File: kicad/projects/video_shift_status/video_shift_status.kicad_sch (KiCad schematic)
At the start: 32 parts, among them J1 peripheral_addr_bus_connector, J2 peripheral_aux_connector, J3 peripheral_membank_connector, U1 74HC245, U10 74HC377, U11 74HC00, U12 74HC04, U2 74HC245, U3 74HC245, U4 74HC245, U5 74HC245, U6 74HC245, U7 74HC245, U8 74HC245, U9 74HC245

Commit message: Bit more tweaking and fleshing out of video circuits.
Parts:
- removed U11: 74HC00, symbol 74xx:74HC00
- removed U12: 74HC04, symbol 74xx:74HC04
- added C12, C13: C, Capacitor_THT:C_Disc_D5.0mm_W2.5mm_P5.00mm, symbol Device:C
- added J4, J5: Conn_01x16_Socket, Connector_PinSocket_2.54mm:PinSocket_1x16_P2.54mm_Horizontal, symbol Connector:Conn_01x16_Socket
- added U11: 74HC138, Package_DIP:DIP-16_W7.62mm_Socket, symbol sixteen-bit-computer:74HC138
- added U13: 74HC10, Package_DIP:DIP-14_W7.62mm_Socket, symbol sixteen-bit-computer:74HC10
- U10, U9: footprint (none) -> Package_DIP:DIP-20_W7.62mm_Socket
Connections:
- net ADDRESSED: now also U13.1, U13.9
- net GND: now also C12.2, C13.1, U11.3 (C), U11.4 (~{G2A}), U11.5 (~{G2B}), U11.8 (GND), U13.7 (GND)
- net MEM_ACT: now also U13.10, U13.2
- net SHIFT_SEL_0: now also U11.1 (A)
- net SHIFT_SEL_1: now also U11.2 (B)
- net VCC: now also C12.1, C13.2, U11.16 (VCC), U11.6 (G1), U13.14 (VCC), U13.4, U13.5
- net ~{READ}: now also U13.8
- net ~{RFM}/WTM: now also U13.13, U13.3
- net ~{WRITE}: now also U13.12
- net ~{SHIFT_2}: now reaches U3.19 (~{OE})
- net ~{SHIFT_2}: now also U7.19 (~{OE}), U11.13 (Y2)
- net ~{SHIFT_0}: now reaches U5.19 (~{OE})
- net ~{SHIFT_0}: now also U1.19 (~{OE}), U11.15 (Y0)
- net ~{SHIFT_1}: now reaches U2.19 (~{OE})
- net ~{SHIFT_1}: now also U6.19 (~{OE}), U11.14 (Y1)
- net ~{SHIFT_3}: now reaches U8.19 (~{OE})
- net ~{SHIFT_3}: now also U4.19 (~{OE}), U11.12 (Y3)
- net ADDR_BUS_00: no longer names the net of J1.17 (A_00)
- net ADDR_BUS_01: no longer names the net of J1.18 (A_01)
- net ADDR_BUS_02: no longer names the net of J1.19 (A_02)
- net ADDR_BUS_03: no longer names the net of J1.20 (A_03)
- net ADDR_BUS_04: no longer names the net of J1.21 (A_04)
- net ADDR_BUS_05: no longer names the net of J1.22 (A_05)
- net ADDR_BUS_06: no longer names the net of J1.23 (A_06)
- net ADDR_BUS_07: no longer names the net of J1.24 (A_07)
- net ADDR_BUS_08: no longer names the net of J1.25 (A_08)
- net ADDR_BUS_09: no longer names the net of J1.26 (A_09)
- net ADDR_BUS_10: no longer names the net of J1.27 (A_10)
- net ADDR_BUS_11: no longer names the net of J1.28 (A_11)
- net ADDR_BUS_12: no longer names the net of J1.29 (A_12)
- net ADDR_BUS_13: no longer names the net of J1.30 (A_13)
- net ADDR_BUS_14: no longer names the net of J1.31 (A_14)
- net ADDR_BUS_15: no longer names the net of J1.32 (A_15)
- net BANK_BUS_00: no longer names the net of J3.1 (B_00)
- net BANK_BUS_01: no longer names the net of J3.2 (B_01)
- net BANK_BUS_02: no longer names the net of J3.3 (B_02)
- net BANK_BUS_03: no longer names the net of J3.4 (B_03)
- net BANK_BUS_04: no longer names the net of J3.5 (B_04)
- net BANK_BUS_05: no longer names the net of J3.6 (B_05)
- net BANK_BUS_06: no longer names the net of J3.7 (B_06)
- net BANK_BUS_07: no longer names the net of J3.8 (B_07)
- net BANK_BUS_08: no longer names the net of J3.9 (B_08)
- net BANK_BUS_09: no longer names the net of J3.10 (B_09)
- net BANK_BUS_10: no longer names the net of J3.11 (B_10)
- net BANK_BUS_11: no longer names the net of J3.12 (B_11)
- net BANK_BUS_12: no longer names the net of J3.13 (B_12)
- net BANK_BUS_13: no longer names the net of J3.14 (B_13)
- net BANK_BUS_14: no longer names the net of J3.15 (B_14)
- net BANK_BUS_15: no longer names the net of J3.16 (B_15)
- net CTL_CLK: no longer names the net of J2.8 (CCLK)
- net DATA_BUS_05: no longer names the net of J1.6 (D_05)
- net DATA_BUS_06: no longer names the net of J1.7 (D_06)
- net DATA_BUS_07: no longer names the net of J1.8 (D_07)
- net DATA_BUS_08: no longer names the net of J1.9 (D_08)
- net DATA_BUS_09: no longer names the net of J1.10 (D_09)
- net DATA_BUS_10: no longer names the net of J1.11 (D_10)
- net DATA_BUS_11: no longer names the net of J1.12 (D_11)
- net DATA_BUS_12: no longer names the net of J1.13 (D_12)
- net DATA_BUS_13: no longer names the net of J1.14 (D_13)
- net DATA_BUS_14: no longer names the net of J1.15 (D_14)
- net DATA_BUS_15: no longer names the net of J1.16 (D_15)
- net RESET: no longer names the net of J2.14 (RST)
- new net RFM/~{WTM}: U13.11, U13.6
- no-connect marks 7 -> 56

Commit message: Adding video aux and some bits and bieces on video boards.
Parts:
- added C14, C15: C, Capacitor_THT:C_Disc_D5.0mm_W2.5mm_P5.00mm, symbol Device:C
- added J6: video_aux, Connector_PinSocket_2.54mm:PinSocket_1x07_P2.54mm_Horizontal, symbol sixteen-bit-computer:video_aux
- added J7: Conn_01x03_Pin, Connector_PinHeader_2.54mm:PinHeader_1x03_P2.54mm_Vertical, symbol Connector:Conn_01x03_Pin
- added J8: Conn_01x04_Socket, Connector_PinSocket_2.54mm:PinSocket_1x04_P2.54mm_Horizontal, symbol Connector:Conn_01x04_Socket
- added J9: Conn_02x06_Odd_Even, Connector_PinHeader_2.54mm:PinHeader_2x06_P2.54mm_Vertical, symbol Connector_Generic:Conn_02x06_Odd_Even
- added R2, R3, R4: 10K, Resistor_THT:R_Axial_DIN0207_L6.3mm_D2.5mm_P10.16mm_Horizontal, symbol Device:R_US
- added U12, U14: 74HC04, Package_DIP:DIP-14_W7.62mm_Socket, symbol 74xx:74HC04
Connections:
- net COL_IN_00 is gone; now on net COL_IN_0: U5.11 (B8)
- net COL_IN_01 is gone; now on net COL_IN_1: U5.12 (B7), U6.11 (B8)
- net COL_IN_02 is gone; now on net COL_IN_2: U5.13 (B6), U6.12 (B7), U7.11 (B8)
- net COL_IN_03 is gone; now on net COL_IN_3: U5.14 (B5), U6.13 (B6), U7.12 (B7), U8.11 (B8)
- net COL_IN_04 is gone; now on net COL_IN_4: U5.15 (B4), U6.14 (B5), U7.13 (B6), U8.12 (B7)
- net COL_IN_05 is gone; now on net COL_IN_5: U5.16 (B3), U6.15 (B4), U7.14 (B5), U8.13 (B6)
- net COL_IN_06 is gone; now on net COL_IN_6: U5.17 (B2), U6.16 (B3), U7.15 (B4), U8.14 (B5)
- net COL_IN_07 is gone; now on net COL_IN_7: U5.18 (B1), U6.17 (B2), U7.16 (B3), U8.15 (B4)
- net COL_OUT_00 is gone; now on net COL_OUT_0: U5.9 (A8), U6.9 (A8), U7.9 (A8), U8.9 (A8)
- net COL_OUT_01 is gone; now on net COL_OUT_1: U5.8 (A7), U6.8 (A7), U7.8 (A7), U8.8 (A7)
- net COL_OUT_02 is gone; now on net COL_OUT_2: U5.7 (A6), U6.7 (A6), U7.7 (A6), U8.7 (A6)
- net COL_OUT_03 is gone; now on net COL_OUT_3: U5.6 (A5), U6.6 (A5), U7.6 (A5), U8.6 (A5)
- net COL_OUT_04 is gone; now on net COL_OUT_4: U5.5 (A3), U6.5 (A3), U7.5 (A3), U8.5 (A3)
- net COL_OUT_05 is gone; now on net COL_OUT_5: U5.4 (A3), U6.4 (A3), U7.4 (A3), U8.4 (A3)
- net COL_OUT_06 is gone; now on net COL_OUT_6: U5.3 (A2), U6.3 (A2), U7.3 (A2), U8.3 (A2)
- net COL_OUT_07 is gone; now on net COL_OUT_7: U5.2 (A1), U6.2 (A1), U7.2 (A1), U8.2 (A1)
- net ROW_IN_00 is gone; now on net ROW_IN_0: U1.11 (B8)
- net ROW_IN_01 is gone; now on net ROW_IN_1: U1.12 (B7), U2.11 (B8)
- net ROW_IN_02 is gone; now on net ROW_IN_2: U1.13 (B6), U2.12 (B7), U3.11 (B8)
- net ROW_IN_03 is gone; now on net ROW_IN_3: U1.14 (B5), U2.13 (B6), U3.12 (B7), U4.11 (B8)
- net ROW_IN_04 is gone; now on net ROW_IN_4: U1.15 (B4), U2.14 (B5), U3.13 (B6), U4.12 (B7)
- net ROW_IN_05 is gone; now on net ROW_IN_5: U1.16 (B3), U2.15 (B4), U3.14 (B5), U4.13 (B6)
- net ROW_IN_06 is gone; now on net ROW_IN_6: U1.17 (B2), U2.16 (B3), U3.15 (B4), U4.14 (B5)
- net ROW_IN_07 is gone; now on net ROW_IN_7: U1.18 (B1), U2.17 (B2), U3.16 (B3), U4.15 (B4)
- net ROW_OUT_00 is gone; now on net ROW_OUT_0: U1.9 (A8), U2.9 (A8), U3.9 (A8), U4.9 (A8)
- net ROW_OUT_01 is gone; now on net ROW_OUT_1: U1.8 (A7), U2.8 (A7), U3.8 (A7), U4.8 (A7)
- net ROW_OUT_02 is gone; now on net ROW_OUT_2: U1.7 (A6), U2.7 (A6), U3.7 (A6), U4.7 (A6)
- net ROW_OUT_03 is gone; now on net ROW_OUT_3: U1.6 (A5), U2.6 (A5), U3.6 (A5), U4.6 (A5)
- net ROW_OUT_04 is gone; now on net ROW_OUT_4: U1.5 (A3), U2.5 (A3), U3.5 (A3), U4.5 (A3)
- net ROW_OUT_05 is gone; now on net ROW_OUT_5: U1.4 (A3), U2.4 (A3), U3.4 (A3), U4.4 (A3)
- net ROW_OUT_06 is gone; now on net ROW_OUT_6: U1.3 (A2), U2.3 (A2), U3.3 (A2), U4.3 (A2)
- net ROW_OUT_07 is gone; now on net ROW_OUT_7: U1.2 (A1), U2.2 (A1), U3.2 (A1), U4.2 (A1)
- net ADDRESSED: now also J8.1 (Pin_1), J8.2 (Pin_2), J8.3 (Pin_3), J8.4 (Pin_4), R4.2
- net BANK_SEL: now also U10.2 (Q0), J6.5 (BANK_SEL); no longer U10.15 (Q5)
- net DATA_BUS_00: now also U10.7 (D2); no longer U10.18 (D7)
- net DATA_BUS_01: now also U10.4 (D1); no longer U10.17 (D6)
- net DATA_BUS_02: now also U10.3 (D0); no longer U10.14 (D5)
- net GND: now also U10.14 (D5), U10.17 (D6), U10.18 (D7), C14.2, C15.2, R2.2, R3.2, R4.1, U12.3, U12.7 (GND), U14.7 (GND); no longer U10.3 (D0), U10.4 (D1), U10.7 (D2)
- net H_BLANK: now also J6.6 (H_BLANK)
- net SHIFT_SEL_0: now also U10.6 (Q2); no longer U10.19 (Q7)
- net SHIFT_SEL_1: now also U10.5 (Q1); no longer U10.16 (Q6)
- net VCC: now also C14.1, C15.1, U12.14 (VCC), U14.14 (VCC)
- net V_BLANK: now also J6.7 (V_BLANK)
- net ROW_OUT_0: now reaches J4.1 (Pin_1)
- net COL_OUT_1: now reaches J4.10 (Pin_10)
- net COL_OUT_2: now reaches J4.11 (Pin_11)
- net COL_OUT_3: now reaches J4.12 (Pin_12)
- net COL_OUT_4: now reaches J4.13 (Pin_13)
- net COL_OUT_5: now reaches J4.14 (Pin_14)
- net COL_OUT_6: now reaches J4.15 (Pin_15)
- net COL_OUT_7: now reaches J4.16 (Pin_16)
- net ROW_OUT_1: now reaches J4.2 (Pin_2)
- net ROW_OUT_2: now reaches J4.3 (Pin_3)
- net ROW_OUT_3: now reaches J4.4 (Pin_4)
- net ROW_OUT_4: now reaches J4.5 (Pin_5)
- net ROW_OUT_5: now reaches J4.6 (Pin_6)
- net ROW_OUT_6: now reaches J4.7 (Pin_7)
- net ROW_OUT_7: now reaches J4.8 (Pin_8)
- net COL_OUT_0: now reaches J4.9 (Pin_9)
- net ROW_IN_0: now reaches J5.1 (Pin_1)
- net COL_IN_1: now reaches J5.10 (Pin_10)
- net COL_IN_2: now reaches J5.11 (Pin_11)
- net COL_IN_3: now reaches J5.12 (Pin_12)
- net COL_IN_4: now reaches J5.13 (Pin_13)
- net COL_IN_5: now reaches J5.14 (Pin_14)
- net COL_IN_6: now reaches J5.15 (Pin_15)
- net COL_IN_7: now reaches J5.16 (Pin_16)
- net ROW_IN_1: now reaches J5.2 (Pin_2)
- net ROW_IN_2: now reaches J5.3 (Pin_3)
- net ROW_IN_3: now reaches J5.4 (Pin_4)
- net ROW_IN_4: now reaches J5.5 (Pin_5)
- net ROW_IN_5: now reaches J5.6 (Pin_6)
- net ROW_IN_6: now reaches J5.7 (Pin_7)
- net ROW_IN_7: now reaches J5.8 (Pin_8)
- net COL_IN_0: now reaches J5.9 (Pin_9)
- new net: U12.10, U12.9
- new net: U12.13, U12.6
- new net: U14.6, U14.9
- new net: U14.2, U14.3
- new net: U14.10, U14.13
- new net CHOSEN_PIX_CLK: J7.2 (Pin_2), J9.2 (Pin_2), R2.1, U12.5
- new net PIX_CLK_DELAY_1: J9.4 (Pin_4), U12.11, U12.12
- new net PIX_CLK_DELAY_2: J9.6 (Pin_6), U12.8, U14.1
- new net PIX_CLK_DELAY_3: J9.8 (Pin_8), U14.4, U14.5
- new net PIX_CLK_DELAY_4: J9.10 (Pin_10), U14.11, U14.8
- new net PIX_CLK_DELAY_5: J9.12 (Pin_12), U14.12
- new net PIX_CLK_MOD: J6.4 (PIX_CLK_MOD), J9.1 (Pin_1), J9.11 (Pin_11), J9.3 (Pin_3), J9.5 (Pin_5), J9.7 (Pin_7), J9.9 (Pin_9), R3.1
- new net PIX_CLK_RAW: J6.3 (PIX_CLK_RAW), J7.3 (Pin_3), U12.1
- new net ~{PIX_CLK_RAW}: J7.1 (Pin_1), U12.2
- no-connect marks 56 -> 59
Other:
- note added: "Addressed input"
- note added: "Pixel clock delay"
- note added: "Shift select"
- moved on the sheet: C1, C10, C11, C12, C13, C2, C3, C4, C5, C6, C7, C8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

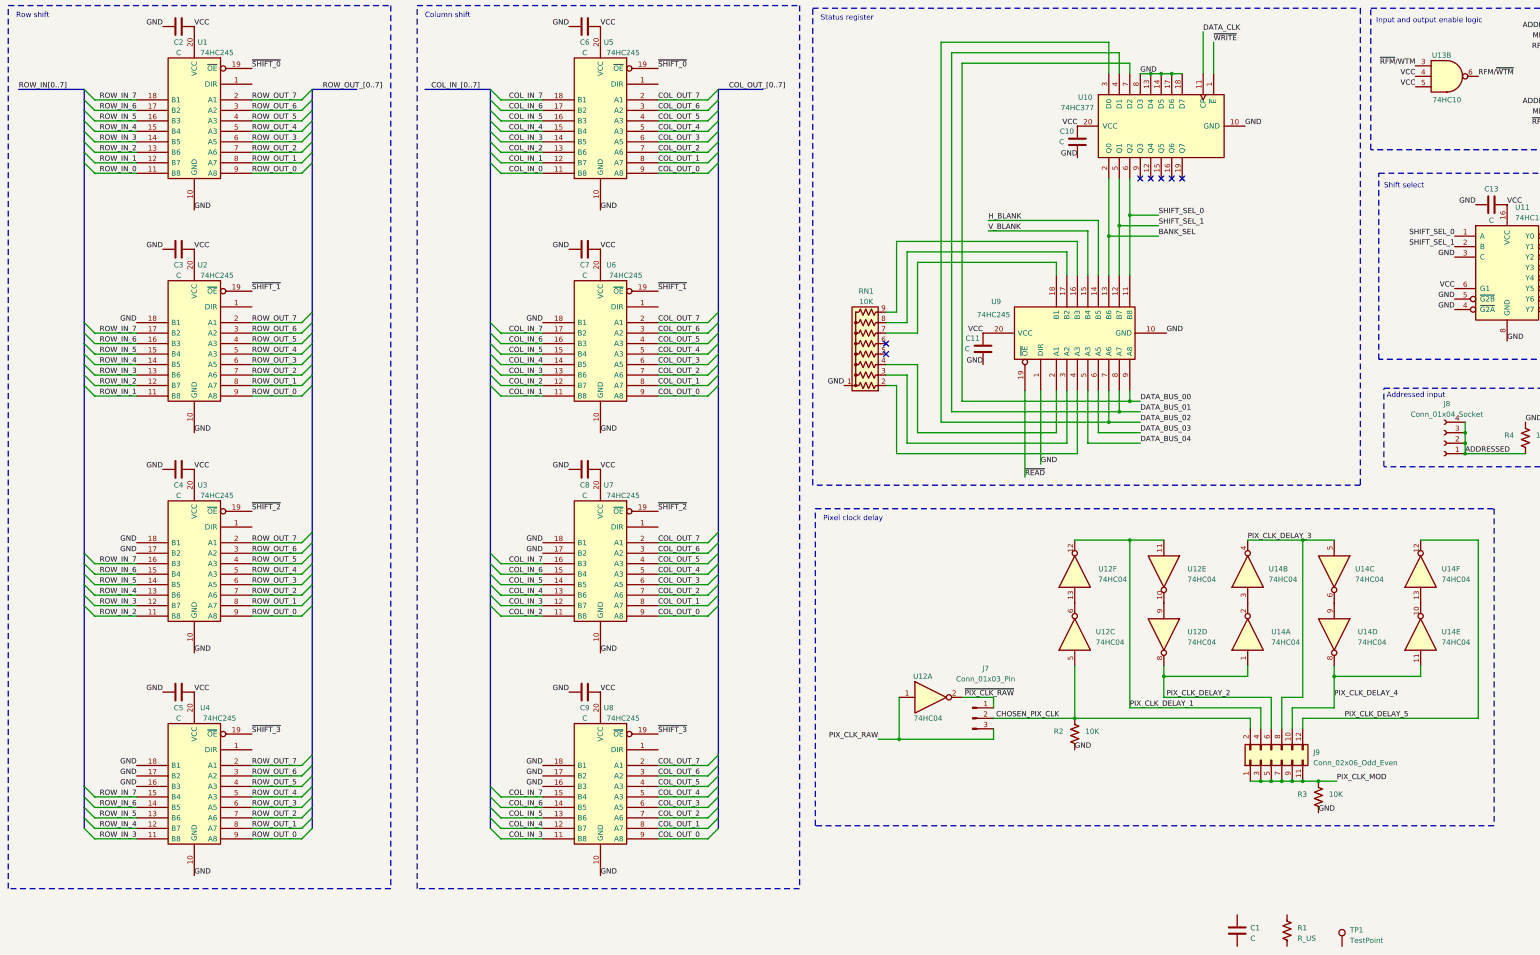
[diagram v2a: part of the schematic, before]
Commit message: Start work on shift status delay PCB.
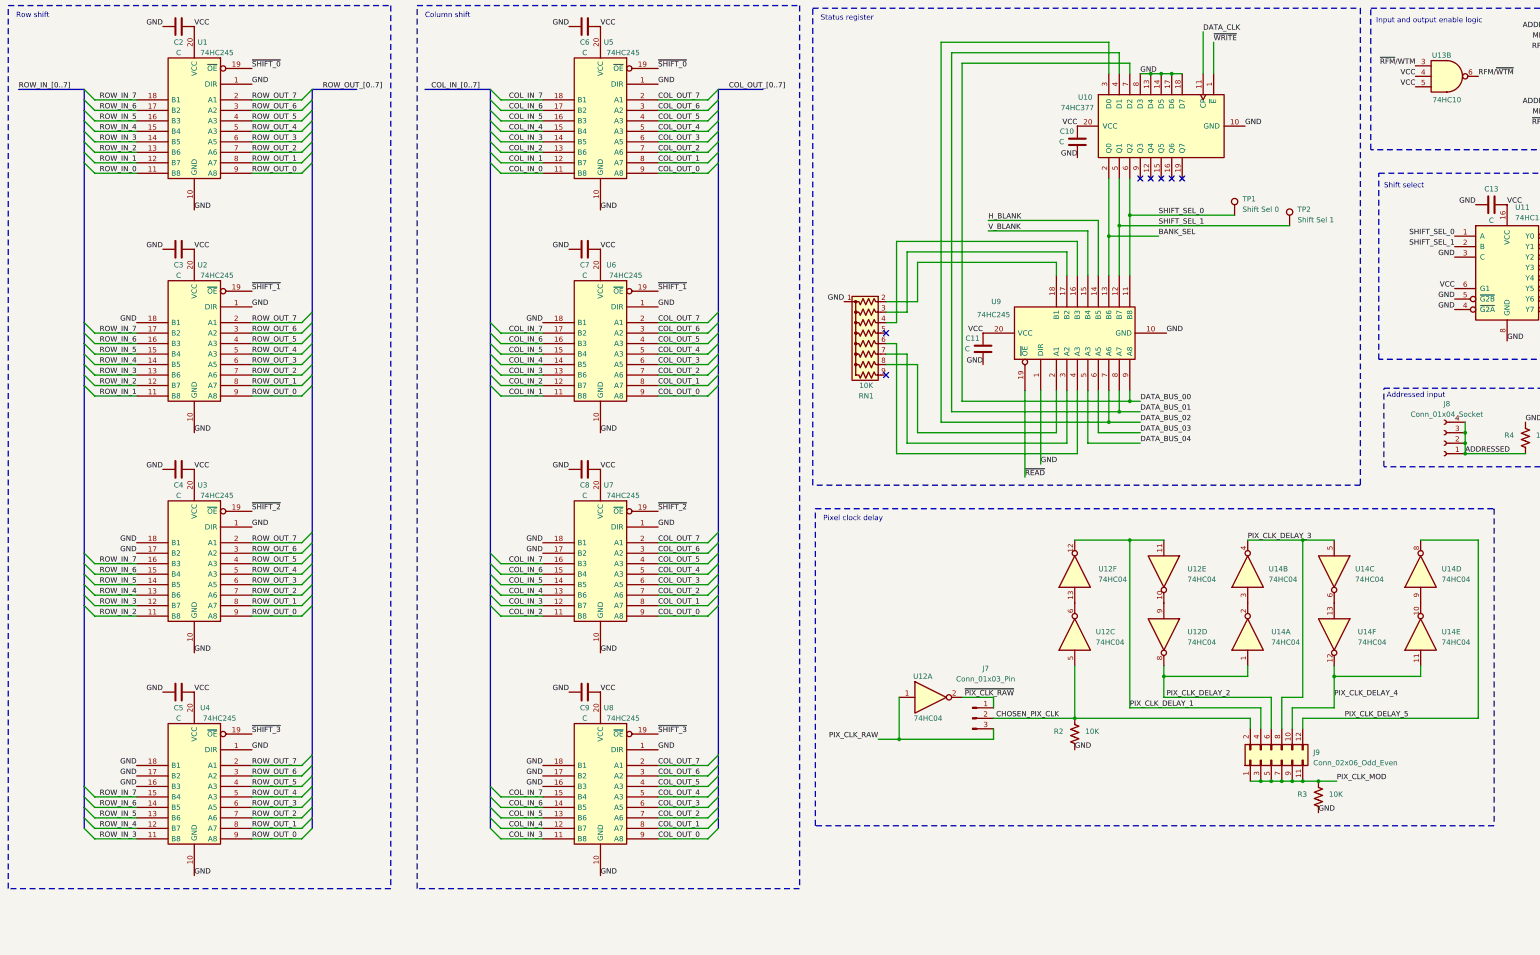
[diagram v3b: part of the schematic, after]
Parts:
- removed C1: C, Capacitor_THT:C_Disc_D5.0mm_W2.5mm_P5.00mm, symbol Device:C
- removed R1: R_US, Resistor_THT:R_Axial_DIN0207_L6.3mm_D2.5mm_P10.16mm_Horizontal, symbol Device:R_US
- added TP2: Shift Sel 1, Connector_Pin:Pin_D1.0mm_L10.0mm, symbol Connector:TestPoint
- TP1: value TestPoint -> Shift Sel 0
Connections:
- net GND: now also U1.1 (DIR), U2.1 (DIR), U3.1 (DIR), U4.1 (DIR), U5.1 (DIR), U6.1 (DIR), U7.1 (DIR), U8.1 (DIR)
- net PIX_CLK_DELAY_4: now also U14.12; no longer U14.8
- net PIX_CLK_DELAY_5: now also U14.8; no longer U14.12
- net SHIFT_SEL_0: now also TP1.1
- net SHIFT_SEL_1: now also TP2.1
- net at U14.6: now also U14.13; no longer U14.9
- net at U9.16 (B3): now also RN1.4 (R3); no longer RN1.9 (R8)
- net at U9.17 (B2): now also RN1.3 (R2); no longer RN1.8 (R7)
- net at U9.18 (B1): now also RN1.2 (R1); no longer RN1.7 (R6)
- net at U9.2 (A1): now also RN1.8 (R7); no longer RN1.4 (R3)
- net at U9.3 (A2): now also RN1.7 (R6); no longer RN1.3 (R2)
- net at U9.4 (A3): now also RN1.6 (R5); no longer RN1.2 (R1)
- net at U14.10: now also U14.9; no longer U14.13
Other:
- moved on the sheet: RN1, TP1, U14D, U14F

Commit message: Add indicator LEDs to shift status delay board. Bit of work on bank sel PCB.
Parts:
- removed TP1: Shift Sel 0, Connector_Pin:Pin_D1.0mm_L10.0mm, symbol Connector:TestPoint
- removed TP2: Shift Sel 1, Connector_Pin:Pin_D1.0mm_L10.0mm, symbol Connector:TestPoint
- added C1: C, Capacitor_THT:C_Disc_D5.0mm_W2.5mm_P5.00mm, symbol Device:C
- added D1, D2, D3: LED, sixteen-bit-computer:LED_D5.0mm_Horizontal_O3.81mm_Z3.0mm, symbol Device:LED
- added R1, R5, R6: R_US, Resistor_THT:R_Axial_DIN0207_L6.3mm_D2.5mm_P10.16mm_Horizontal, symbol Device:R_US
- added U15: 74HC08, Package_DIP:DIP-14_W7.62mm_Socket, symbol sixteen-bit-computer:74HC08
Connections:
- net BANK_SEL: now also U15.1, U15.2
- net GND: now also C1.2, R1.2, R5.2, R6.2, U15.12, U15.13, U15.7 (GND)
- net SHIFT_SEL_0: now also U15.4, U15.5
- net SHIFT_SEL_1: now also U15.10, U15.9
- net VCC: now also C1.1, U15.14 (VCC)
- new net: D2.1 (K), R5.1
- new net: D1.1 (K), R1.1
- new net: D3.1 (K), R6.1
- new net BANK_SEL_LED: D1.2 (A), U15.3
- new net SHIFT_SEL_0_LED: D2.2 (A), U15.6
- new net SHIFT_SEL_1_LED: D3.2 (A), U15.8
- no-connect marks 59 -> 60
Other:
- note added: "Status display"
